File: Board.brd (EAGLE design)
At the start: 73 x 65.1 mm, 34 parts, among them IC1 LM339N, Q1 IRFZ48n, Q2 IRFZ48n, Q3 IRFZ48n, Q4 IRFZ48n, Q5 BC337, X1 12Vcc IN, X2 MOTOR DC

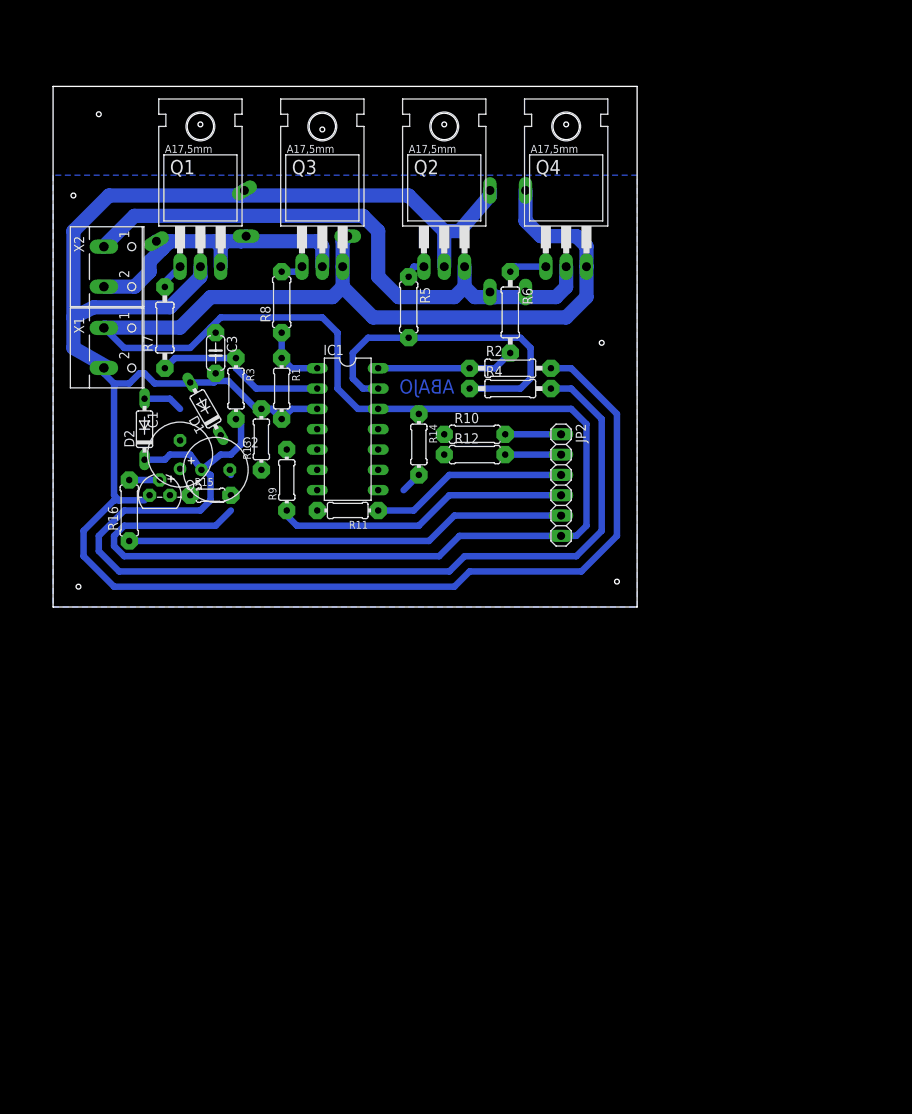
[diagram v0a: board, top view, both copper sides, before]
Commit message: Ver 2
Board: A new design using a IC H bridge driver properly calculated for the motor and mosfets.
Algorithm: An algorithm that use a 3 axis gyro to balance itself.
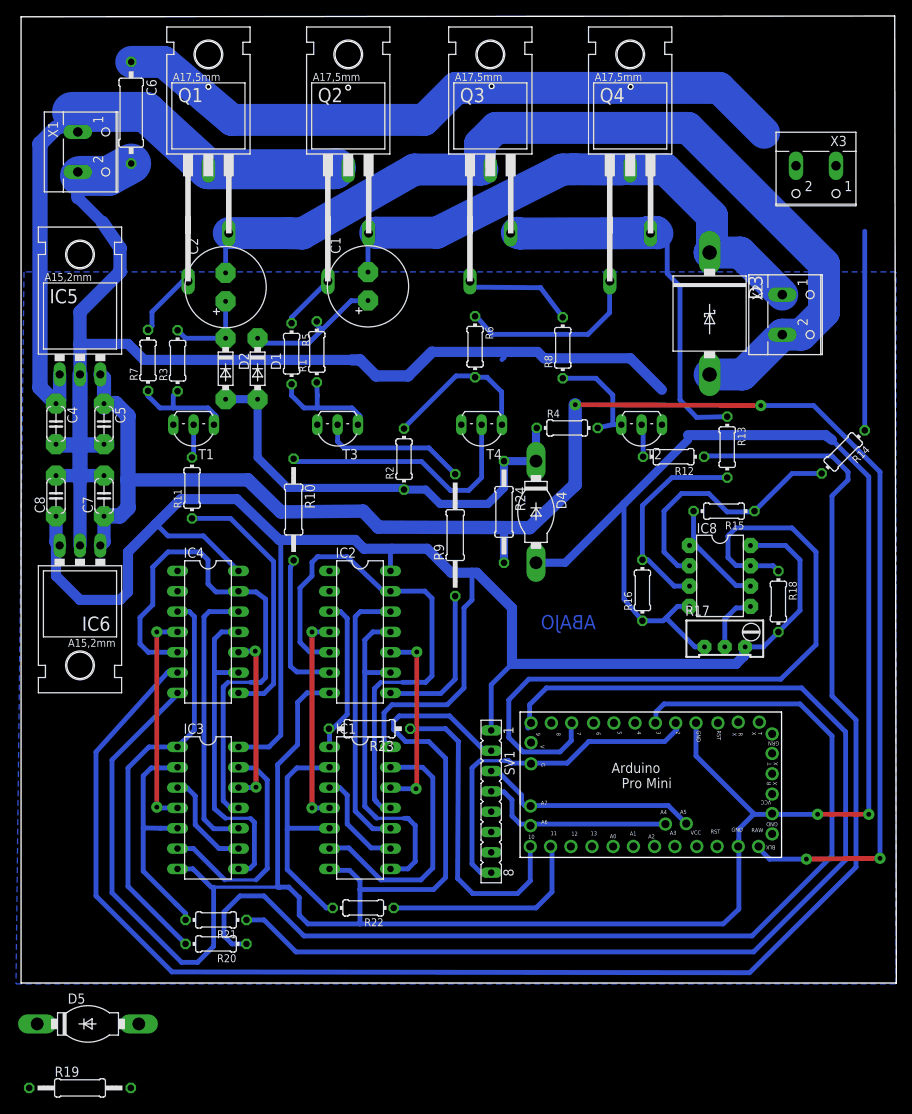
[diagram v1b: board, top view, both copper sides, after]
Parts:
- removed C3: (no value), rcl:C050-024X044
- removed D6: 1N5060GP, diode:DO15-12
- removed JP2: (no value), pinhead:1X06
- removed Q5: BC337, transistor-npn:TO92
- added C4, C5, C7, C8: (no value), rcl:C050-024X044
- added C6: Polyswitch 20A, rcl:0309/12
- added IC2, IC4: 74AC04N, 74xx-eu:DIL14
- added IC3: 74AC08N, 74xx-eu:DIL14
- added IC5, IC6: (no value), v-reg:78XXL
- added IC8: LM358N, linear:DIL08
- added R17: (no value), rcl:RTRIM64W
- added R18: 1k, rcl:0204/7
- added R19, R24: 270, rcl:0207/12
- added R20, R21, R22: 330, rcl:0204/7
- added R23: 330, rcl:0207/10
- added SV1: MPU6050, con-lsta:FE08
- added T1, T2, T3, T4: (no value), transistor:TO92-CBE
- added U$1: ARDUINO_MINI_PRO+AZUL, E14_Arduino_victor:ARDUINO_MINI_PRO+AZUL
- added X3: Resistencia Shunt, con-wago-500:W237-102
- C1, C2: value 100uF -> (none); device rcl:E3,5-8 -> rcl:E3,5-10
- D1, D2: value 1N4148DO35-7 -> 1N5817-B; device diode:DO35-7 -> diode:DO41-7.6
- D3: value 1N5060GP -> BZW50B; device diode:DO15-12 -> diode:AG
- D4, D5: value 1N5060GP -> zener 5.1V; device diode:DO15-12 -> diode:SOD83-12
- IC1: value LM339N -> 74ALS09N; device linear:DIL14 -> 74xx-eu:DIL14
- Q1, Q2, Q3, Q4: value IRFZ48n -> IRF3205
- R1: value 4k7 -> 10k
- R10: value 330 -> 3k3; device rcl:0207/7 -> rcl:0207/12
- R11: value 330 -> 3k3
- R12: value 330 -> 3k3; device rcl:0207/7 -> rcl:0204/7
- R13, R3: value 27k -> 10k
- R15: value 1k5 -> 10k; device rcl:0204/5 -> rcl:0204/7
- R16: value 330 -> 10k; device rcl:0207/7 -> rcl:0204/7
- R2: value 4k7 -> 10k; device rcl:0207/10 -> rcl:0204/7
- R4: value 27k -> 10k; device rcl:0207/10 -> rcl:0204/7
- R5, R8: value 10 -> 1k; device rcl:0207/7 -> rcl:0204/7
- R6, R7: value 10 -> 1k; device rcl:0207/10 -> rcl:0204/7
- R9: value 330 -> 3k3; device rcl:0204/7 -> rcl:0207/15
- X1: value 12Vcc IN -> (none)
- moved D5 112.1 mm to (5.00, -21.0), flipped to the top, turned to 0 degrees
- moved X2 85.0 mm to (93.1, 67.7)
- moved R16 64.9 mm to (74.3, 33.2)
- moved D3 64.8 mm to (82.7, 67.8), flipped to the top, turned to 270 degrees
- moved R15 64.2 mm to (84.5, 43.1), turned to 180 degrees
- moved R13 58.2 mm to (84.9, 51.1), turned to 270 degrees
- moved R14 53.1 mm to (99.4, 50.5), turned to 225 degrees
- moved IC1 47.4 mm to (39.0, 6.00)
- moved D4 45.6 mm to (61.0, 43.0), flipped to the top, turned to 270 degrees
- moved R8 35.6 mm to (64.3, 63.5)
- moved C1 31.5 mm to (40.0, 71.2)
- moved R12 24.9 mm to (78.2, 49.9), turned to 180 degrees
- moved X1 24.7 mm to (5.00, 88.0)
- moved R10 24.5 mm to (30.7, 43.3), turned to 270 degrees
- moved C2 22.9 mm to (22.2, 71.1), turned to 90 degrees
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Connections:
- removed net +15V: C2.+, D2.C, R3.2, R4.2
- removed net +3V3: IC1.11, IC1.5, IC1.7, IC1.9, R13.1, R14.2
- removed net N$22: C1.-, Q5.3, R15.2
- removed net N$5: IC1.14, R2.1, R6.2
- new net !SD1: R21.1, U$1.9
- new net !SD2: IC1.2, IC1.5, R22.2
- new net +24V: C4.1, IC5.IN, Q1.2, Q2.2, X1.1
- new net +5V: C8.1, IC1.14, IC2.14, IC3.14, IC4.14, IC6.OUT, IC8.8, R17.3, R18.2, SV1.1
- new net +7V: D1.A, D2.A, D4.C, D5.C, R19.1, R2.1, R24.1, R4.1
- new net IN1: R20.1, U$1.3
- new net IN2: R23.1, U$1.10
- new net N$23: IC1.4, IC2.4
- new net N$24: IC8.5, R17.2
- new net N$25: R2.2, R6.2, T4.C
- new net N$26: R10.1, T4.B
- new net N$27: R4.2, R8.1, T2.C
- new net N$28: IC3.11, IC4.13, IC4.5
- new net N$29: IC3.12, IC4.10
- new net N$30: IC3.10, IC4.12
- new net N$31: IC3.3, IC3.9
- new net N$32: IC3.13, IC3.6
- new net N$33: IC8.3, R13.2, R16.2
- new net N$34: IC3.4, IC4.4
- new net N$35: IC8.2, R14.2, R15.1
- new net N$36: R3.1, R7.1, T1.C
- new net N$37: SV1.8, U$1.2
- new net N$38: IC8.1, IC8.6, R15.2
- new net N$39: R11.2, T1.B
- new net N$40: IC8.7, R18.1, U$1.7
- new net N$41: R12.2, T2.B
- new net N$43: C6.1, R14.1, X3.2
- new net N$44: IC3.1, IC4.3, R20.2
- new net N$45: IC3.2, IC3.5, R21.2
- new net N$47: IC1.1, IC2.3, R23.2
- new net N$49: R22.1, U$1.11
- new net N$53: IC2.6, R10.2
- new net N$54: IC2.8, R9.1
- new net N$55: IC4.8, R11.1
- new net N$56: IC1.11, IC2.13, IC2.5
- net +12V: now also C5.1, C7.1, IC5.OUT, IC6.IN, R19.2, R24.2, U$1.RAW; no longer C3.2, D1.A, D3.C, D6.C, IC1.3, Q1.2, Q2.2, R1.2, R13.2, R15.1, R2.2, X1.2
- net GND: now also C4.2, C5.2, C6.2, C7.2, C8.2, IC1.7, IC2.7, IC3.7, IC4.7, IC5.GND, IC6.GND, IC8.4, R16.1, R17.1, SV1.2, T1.E, T2.E, T3.E, T4.E, U$1.GND, U$1.GND., U$1.GND.., X1.2; no longer C2.-, C3.1, IC1.12, JP2.6, Q3.3, Q4.3, Q5.1, R14.1, X1.1
- net N$1: now also C1.+, D1.C, R1.2; no longer IC1.2, R3.1, R7.1
- net N$10: now also IC4.6; no longer IC1.8
- net N$12: now also R9.2, T3.B; no longer IC1.6, R11.2
- net N$13: now also C2.-; no longer D4.C
- net N$14: now also IC1.12, IC2.10; no longer JP2.4, R9.1
- net N$15: now also SV1.3, U$1.A5; no longer JP2.1, R10.2
- net N$16: now also C1.-, D3.C; no longer D5.C, D6.A
- net N$17: now also IC1.10, IC2.12; no longer JP2.3, R11.1
- net N$18: now also Q3.3, Q4.3, R13.1, X3.1; no longer JP2.2, R12.2
- net N$19: now also IC1.13, IC1.6; no longer C1.+, D1.C, D2.A
- net N$2: now also C2.+, D2.C, R3.2; no longer IC1.13, R4.1, R5.2
- net N$20: now also IC1.3, IC1.9; no longer Q5.2, R16.2
- net N$21: now also SV1.4, U$1.A4; no longer JP2.5, R16.1
- net N$6: now also IC3.8, IC4.11, IC4.9; no longer IC1.1, R1.1, R8.1
- net N$7: now also R1.1, R5.2, T3.C; no longer IC1.4, R9.2
- net N$8: now also IC1.8, IC2.11, IC2.9; no longer IC1.10, R10.1
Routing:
- net GND: track 256.6 -> 530.9 mm, vias 0 -> 2
- net +5V: track 0.00 -> 225.2 mm
- net N$10: track 0.00 -> 207.5 mm
- net !SD1: track 0.00 -> 143.7 mm
- net IN1: track 0.00 -> 129.8 mm
- net +15V: track 128.0 -> 0.00 mm
- net N$43: track 0.00 -> 110.6 mm
- net N$40: track 0.00 -> 91.3 mm
- net +24V: track 0.00 -> 88.3 mm
- net N$13: track 38.4 -> 118.9 mm
- net N$28: track 0.00 -> 66.5 mm
- net N$56: track 0.00 -> 66.1 mm
- net +7V: track 0.00 -> 56.9 mm
- net N$44: track 0.00 -> 52.8 mm
- net +12V: track 258.9 -> 211.2 mm, vias 0 -> 4
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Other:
- board size 73 x 65.1 mm -> 109.4 x 120.9 mm

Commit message: Ver 3
Board: Some adjustments at the design.
Algorithm:  Adjustments too.
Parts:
- removed IC3: 74AC08N, 74xx-eu:DIL14
- removed IC4: 74AC04N, 74xx-eu:DIL14
- removed IC5, IC6: (no value), v-reg:78XXL
- removed IC8: LM358N, linear:DIL08
- removed R18: 1k, rcl:0204/7
- removed R19, R24: 270, rcl:0207/12
- removed R20, R21, R22: 330, rcl:0204/7
- removed R23: 330, rcl:0207/10
- removed T1, T2, T3, T4: (no value), transistor:TO92-CBE
- removed X3: Resistencia Shunt, con-wago-500:W237-102
- added C3: (no value), rcl:C050-030X075
- added D6, D7, D8: 1N4148DO35-10, diode:DO35-10
- added D9: 15KEXXC, diode:CB429-17
- added JP1: (no value), pinhead:1X06
- added SJ1: (no value), jumper:SJW
- added U$2, U$3: IR2104, IR2104:IR2104
- C1: value (none) -> 1uF; device rcl:E3,5-10 -> rcl:E3,5-8
- C2: value (none) -> 220nF; device rcl:E3,5-10 -> rcl:C075-032X103
- C4: device rcl:C050-024X044 -> rcl:E3,5-8
- C5: value (none) -> 220nF; device rcl:C050-024X044 -> rcl:C075-032X103
- C6: device rcl:0309/12 -> rcl:C075-032X103
- C7: value (none) -> 330nF
- C8: value (none) -> 100nF
- D1, D2: value 1N5817-B -> 1N4148DO35-10; device diode:DO41-7.6 -> diode:DO35-10
- D3: value BZW50B -> 1N4148DO35-10; device diode:AG -> diode:DO35-10
- D4, D5: value zener 5.1V -> 1N4148DO35-10; device diode:SOD83-12 -> diode:DO35-10
- IC1: value 74ALS09N -> (none); device 74xx-eu:DIL14 -> v-reg:78XXL
- IC2: value 74AC04N -> LM358N; device 74xx-eu:DIL14 -> linear:DIL08
- Q1, Q2, Q3, Q4: device transistor-fet:TO220 -> transistor-fet Victor:TO220
- R1, R2, R3: value 10k -> 330
- R10: value 3k3 -> (none); device rcl:0207/12 -> rcl_Victor:0204/7
- R11, R12: value 3k3 -> (none); device rcl:0204/7 -> rcl_Victor:0204/7
- R13, R4: value 10k -> (none); device rcl:0204/7 -> rcl_Victor:0204/7
- R14: value 10k -> (none); device rcl:0204/7 -> rcl_Victor:RTRIM64W
- R15: value 10k -> RESISTENCIA SHUNT; device rcl:0204/7 -> resistor:0922V
- R16: value 10k -> 1k; device rcl:0204/7 -> rcl:0207/10
- R17: value (none) -> 1k; device rcl:RTRIM64W -> rcl:0207/10
- R5: value 1k -> 10; device rcl:0204/7 -> rcl:0207/12
- R6, R7: value 1k -> 10; device rcl:0204/7 -> rcl:0207/10
- R8: value 1k -> 10; device rcl:0204/7 -> rcl:0207/15
- R9: value 3k3 -> 330; device rcl:0207/15 -> rcl:0207/10
- X1: value (none) -> 12Vcc IN
- moved R17 163.6 mm to (-37.0, -82.0), turned to 0 degrees
- moved R16 156.6 mm to (-37.0, -77.0), turned to 0 degrees
- moved D3 152.5 mm to (-36.0, -28.0), turned to 0 degrees
- moved R14 150.3 mm to (-39.0, -8.00), turned to 0 degrees
- moved R15 133.4 mm to (-33.0, -20.0), turned to 0 degrees
- moved R13 129.8 mm to (-28.0, -13.0), turned to 0 degrees
- moved D4 124.5 mm to (-36.0, -35.0), turned to 0 degrees
- moved R12 121.4 mm to (-28.0, -9.00), turned to 0 degrees
- moved R4 105.7 mm to (-28.0, 3.00)
- moved R10 73.5 mm to (-28.0, -1.00), turned to 0 degrees
- moved R11 68.7 mm to (-28.0, -5.00), turned to 0 degrees
- moved IC2 68.2 mm to (-27.0, 11.0), turned to 0 degrees
- moved C6 49.7 mm to (55.0, 71.0)
- moved D5 46.1 mm to (-36.0, -42.0)
- moved IC1 42.2 mm to (12.2, 38.6), turned to 90 degrees
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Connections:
- removed net !SD1: R21.1, U$1.9
- removed net !SD2: IC1.2, IC1.5, R22.2
- removed net +7V: D1.A, D2.A, D4.C, D5.C, R19.1, R2.1, R24.1, R4.1
- removed net IN1: R20.1, U$1.3
- removed net IN2: R23.1, U$1.10
- removed net N$12: R9.2, T3.B
- removed net N$14: IC1.12, IC2.10
- removed net N$17: IC1.10, IC2.12
- removed net N$29: IC3.12, IC4.10
- removed net N$30: IC3.10, IC4.12
- removed net N$35: IC8.2, R14.2, R15.1
- removed net N$36: R3.1, R7.1, T1.C
- removed net N$38: IC8.1, IC8.6, R15.2
- removed net N$39: R11.2, T1.B
- removed net N$40: IC8.7, R18.1, U$1.7
- removed net N$41: R12.2, T2.B
- removed net N$43: C6.1, R14.1, X3.2
- removed net N$44: IC3.1, IC4.3, R20.2
- removed net N$45: IC3.2, IC3.5, R21.2
- removed net N$47: IC1.1, IC2.3, R23.2
- removed net N$49: R22.1, U$1.11
- removed net N$53: IC2.6, R10.2
- removed net N$54: IC2.8, R9.1
- removed net N$55: IC4.8, R11.1
- removed net N$56: IC1.11, IC2.13, IC2.5
- new net N$22: IC2.1, IC2.6, R11.2
- new net N$48: JP1.6, U$1.BLK
- new net N$5: R2.2, U$3.2
- new net N$50: JP1.3, U$1.RX.
- new net N$51: JP1.2, U$1.TX.
- new net N$52: JP1.1, U$1.GRN
- net +12V: now also C1.+, C4.+, C8.1, D1.A, D2.A, IC1.OUT, SJ1.2, U$2.1, U$3.1; no longer C5.1, C7.1, IC5.OUT, IC6.IN, R19.2, R24.2
- net +24V: now also C3.2, C7.1, IC1.IN, SJ1.1, X1.2; no longer C4.1, IC5.IN, X1.1
- net +5V: now also IC2.8, JP1.4, R12.2, R14.3, U$1.VCC.; no longer C8.1, IC1.14, IC2.14, IC3.14, IC4.14, IC6.OUT, IC8.8, R17.3, R18.2
- net GND: now also C1.-, C3.1, C4.-, IC1.GND, IC2.4, JP1.5, R13.1, R14.1, U$2.4, U$3.4, X1.1; no longer C4.2, C5.2, D4.A, D5.A, IC1.7, IC2.7, IC3.7, IC4.7, IC5.GND, IC6.GND, IC8.4, R16.1, R17.1, T1.E, T2.E, T3.E, T4.E, X1.2
- net N$1: now also R9.2, U$2.2; no longer C1.+, D1.C, R1.2
- net N$10: now also R9.1, U$1.3; no longer IC4.6, R12.1
- net N$11: now also D8.A, Q4.1; no longer Q3.1
- net N$13: now also C2.2, D9.A, R16.1, U$2.6; no longer C2.-, D3.A
- net N$16: now also C5.2, D9.C, R17.1, U$3.6; no longer C1.-, D3.C
- net N$18: now also R15.2, R4.1; no longer R13.1, X3.1
- net N$19: now also R2.1, U$1.10; no longer IC1.13, IC1.6
- net N$2: now also C2.1, D1.C, U$2.8; no longer C2.+, D2.C, R3.2
- net N$20: now also C5.1, D2.C, U$3.8; no longer IC1.3, IC1.9
- net N$23: now also D5.C, R7.1, U$2.7; no longer IC1.4, IC2.4
- net N$24: now also D7.C, R6.2, U$2.5; no longer IC8.5, R17.2
- net N$25: now also D8.C, R8.1, U$3.5; no longer R2.2, R6.2, T4.C
- net N$26: now also D6.C, R5.2, U$3.7; no longer R10.1, T4.B
- net N$27: now also IC2.3, R13.2; no longer R8.1, T2.C
- net N$28: now also D3.A, R1.2, U$2.3; no longer IC3.11, IC4.13, IC4.5
- net N$3: now also D5.A, R16.2
- net N$31: now also IC2.2, R10.2, R11.1; no longer IC3.3, IC3.9
- net N$32: now also IC2.5, R14.2; no longer IC3.13, IC3.6
- net N$33: now also R3.1, U$1.11; no longer IC8.3, R13.2, R16.2
- net N$34: now also C6.1, R10.1, R15.1; no longer IC3.4, IC4.4
- net N$4: now also D6.A, R17.2
- net N$6: now also D4.A, R3.2, U$3.3; no longer IC3.8, IC4.11, IC4.9
- net N$7: now also U$1.9; no longer R5.2, T3.C
- net N$8: now also D3.C, D4.C, IC2.7, R12.1; no longer IC1.8, IC2.11, IC2.9
- net N$9: now also D7.A, Q3.1; no longer Q4.1
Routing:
- net GND: track 530.9 -> 250.5 mm, vias 2 -> 0
- net N$10: track 207.5 -> 0.00 mm
- net !SD1: track 143.7 -> 0.00 mm
- net +5V: track 225.2 -> 89.6 mm
- net IN1: track 129.8 -> 0.00 mm
- net N$43: track 110.6 -> 0.00 mm
- net N$40: track 91.3 -> 0.00 mm, vias 0 -> 1
- net N$56: track 66.1 -> 0.00 mm
- net +7V: track 56.9 -> 0.00 mm
- net N$44: track 52.8 -> 0.00 mm
- net N$1: track 17.6 -> 65.7 mm
- net N$8: track 42.9 -> 0.00 mm
- net N$16: track 68.5 -> 108.8 mm, vias 0 -> 2
- net IN2: track 38.6 -> 0.00 mm
- net +12V: track 211.2 -> 173.1 mm, vias 4 -> 1
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- added copper zone on layer 16, net N$14
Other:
- board size 109.4 x 120.9 mm -> 99.5 x 76.8 mm

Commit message: Ver 4
Board: I made a mistake and the mosfets weren't as robust as the motor require, so i put two in parallel by vertex of the H bridge (8 in total ).
Algorithm: Some adjustments at parameters.
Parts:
- removed SJ1: (no value), jumper:SJW
- added D10, D11: (no value), diode Victor:DO34Z7
- added F1: FUSEBLANK_5X20MM, fuse:FUSE_HOLDER_5X20MM
- added Q5, Q6, Q7, Q8: IRF3205, transistor-power:TO220BV
- added R18: (no value), rcl_Victor:0204/7
- added X3: Resistencia Shunt, con-wago-500:W237-102
- C1: value 1uF -> 4.7uF
- C2, C5: value 220nF -> 470nF
- C4: value (none) -> 4.7uF
- C6: value Polyswitch 20A -> (none); device rcl:C075-032X103 -> rcl_Victor:E5-13
- D1: value 1N4148DO35-10 -> 1N821; device diode:DO35-10 -> diode:DO35Z10
- D2, D3, D4, D8: value 1N4148DO35-10 -> 1N4148DO35-7; device diode:DO35-10 -> diode:DO35-7
- D5: value 1N4148DO35-10 -> 1N4148DO35-7; device diode:DO35-10 -> diode Victor:DO35-7
- D6: value 1N4148DO35-10 -> 1N4446
- D9: value 15KEXXC -> BR210; device diode:CB429-17 -> diode:BR210S
- Q1, Q2, Q3, Q4: device transistor-fet Victor:TO220 -> transistor-power:TO220BV
- R15: value RESISTENCIA SHUNT -> (none); device resistor:0922V -> rcl_Victor:0204/7
- R16, R9: device rcl:0207/10 -> rcl_Victor:0207/10
- R17, R7: device rcl:0207/10 -> rcl_Victor:0204/7
- R2, R3: device rcl:0204/7 -> rcl_Victor:0207/12
- R5: device rcl:0207/12 -> rcl_Victor:0207/12
- R6: device rcl:0207/10 -> rcl_Victor:0207/12
- R8: device rcl:0207/15 -> rcl_Victor:0204/7
- moved D8 203.5 mm to (73.3, 108.7), turned to 90 degrees
- moved R17 203.0 mm to (38.9, 106.3), turned to 315 degrees
- moved D9 197.8 mm to (30.5, 116.7)
- moved R16 183.1 mm to (-15.8, 104.9), turned to 90 degrees
- moved D6 172.8 mm to (50.4, 100.6), turned to 135 degrees
- moved D7 169.2 mm to (17.9, 104.4), turned to 90 degrees
- moved R13 168.0 mm to (90.8, 105.8), turned to 270 degrees
- moved R14 158.3 mm to (82.0, 94.0)
- moved R4 152.9 mm to (85.3, 105.6), turned to 270 degrees
- moved D5 152.7 mm to (-11.7, 108.8), turned to 90 degrees
- moved R12 140.1 mm to (67.0, 94.0), turned to 90 degrees
- moved R10 135.1 mm to (77.0, 84.0), turned to 180 degrees
- moved R11 133.7 mm to (69.0, 87.0), turned to 180 degrees
- moved D4 131.5 mm to (32.6, 77.2), turned to 90 degrees
- moved IC2 130.7 mm to (74.0, 94.0)
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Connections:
- removed net N$34: C6.1, R10.1, R15.1
- new net N$14: D5.A, Q1.G, Q5.G, R16.2, R7.2
- new net N$17: D1.A, D10.C, R15.2
- new net N$29: D11.C, D2.A, R18.1
- net +12V: now also R15.1, R18.2; no longer D1.A, D2.A, SJ1.2
- net +24V: now also C6.+, Q1.D, Q2.D, Q5.D, Q6.D; no longer Q1.2, Q2.2, SJ1.1
- net GND: now also C6.-, D10.A, D11.A, R10.1, X3.1; no longer C6.2
- net N$11: now also Q4.G, Q8.G; no longer Q4.1
- net N$13: now also D9.T1, Q1.S, Q3.D, Q5.S, Q7.D; no longer D9.A, Q1.3, Q3.2
- net N$16: now also D9.T2, Q2.S, Q4.D, Q6.S, Q8.D; no longer D9.C, Q2.3, Q4.2
- net N$18: now also F1.2, Q3.S, Q4.S, Q7.S, Q8.S; no longer Q3.3, Q4.3, R15.2, R4.1
- net N$3: now also F1.1, R4.1, X3.2; no longer D5.A, Q1.1, R16.2, R7.2
- net N$4: now also Q2.G, Q6.G; no longer Q2.1
- net N$9: now also Q3.G, Q7.G; no longer Q3.1
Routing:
- net GND: track 250.5 -> 443.9 mm, vias 0 -> 4
- net N$8: track 0.00 -> 89.9 mm
- net +24V: track 111.2 -> 183.0 mm
- net N$13: track 104.1 -> 165.5 mm, vias 2 -> 0
- net N$16: track 108.8 -> 165.7 mm, vias 2 -> 0
- net N$7: track 0.00 -> 44.7 mm
- net N$27: track 0.00 -> 34.5 mm
- net +5V: track 89.6 -> 124.2 mm, vias 0 -> 2
- net N$23: track 8.84 -> 43.2 mm
- net N$3: track 0.00 -> 32.7 mm
- net N$26: track 8.87 -> 40.6 mm
- net N$28: track 44.9 -> 71.2 mm
- net N$4: track 2.77 -> 27.7 mm, vias 0 -> 2
- net N$18: track 55.2 -> 76.8 mm
- net N$24: track 37.2 -> 17.0 mm
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- removed copper zone on layer 16, net GND
- removed copper zone on layer 16, net N$14
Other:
- board size 99.5 x 76.8 mm -> 115.7 x 77.4 mm
